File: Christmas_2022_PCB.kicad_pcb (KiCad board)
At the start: 2 copper layers, 61.4 x 60.5 mm, 45 parts, among them J1 USB_A, J2 SOP8_test_point, J3 SOP8_test_point, SW1 SW_Push, SW2 SW_Push, SW3 SW_SPDT, U1 STM32F030K6Tx, U2 AMS1117-3.3

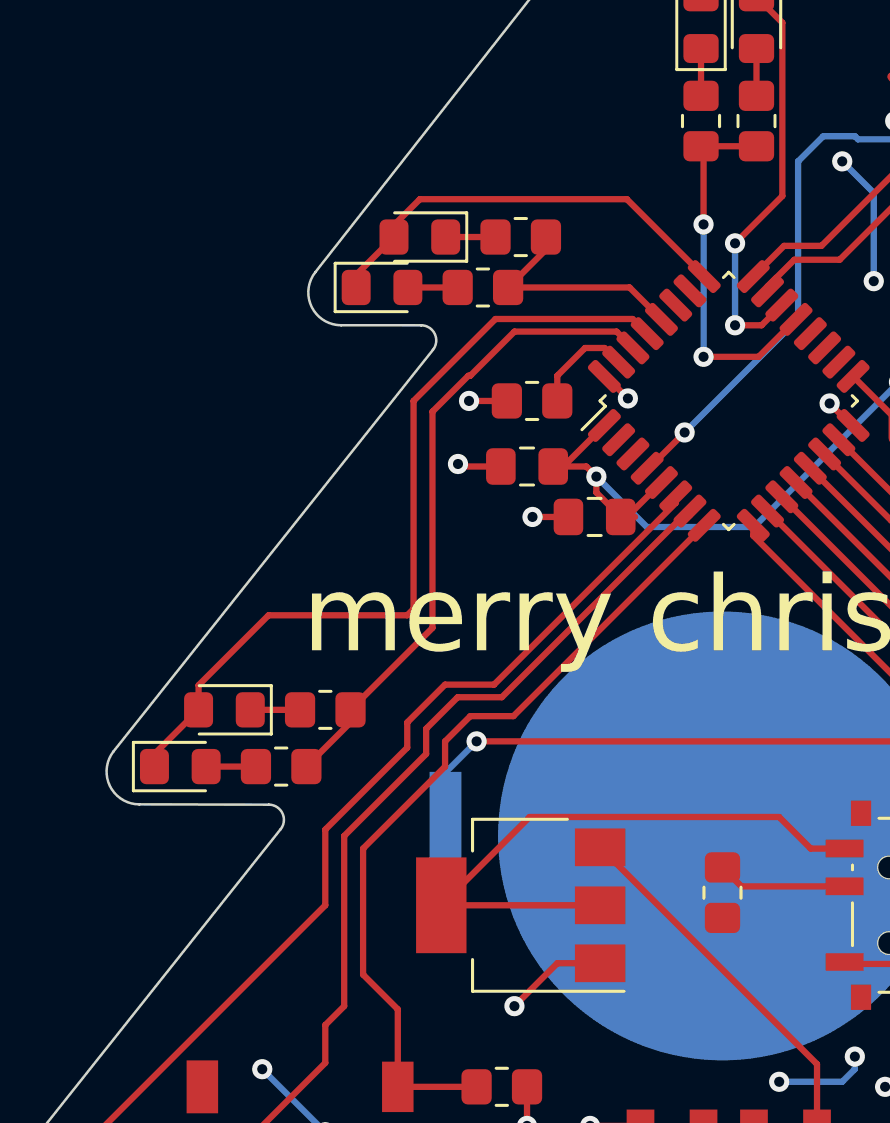
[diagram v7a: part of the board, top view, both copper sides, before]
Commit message: modified VCC pour to balance copper
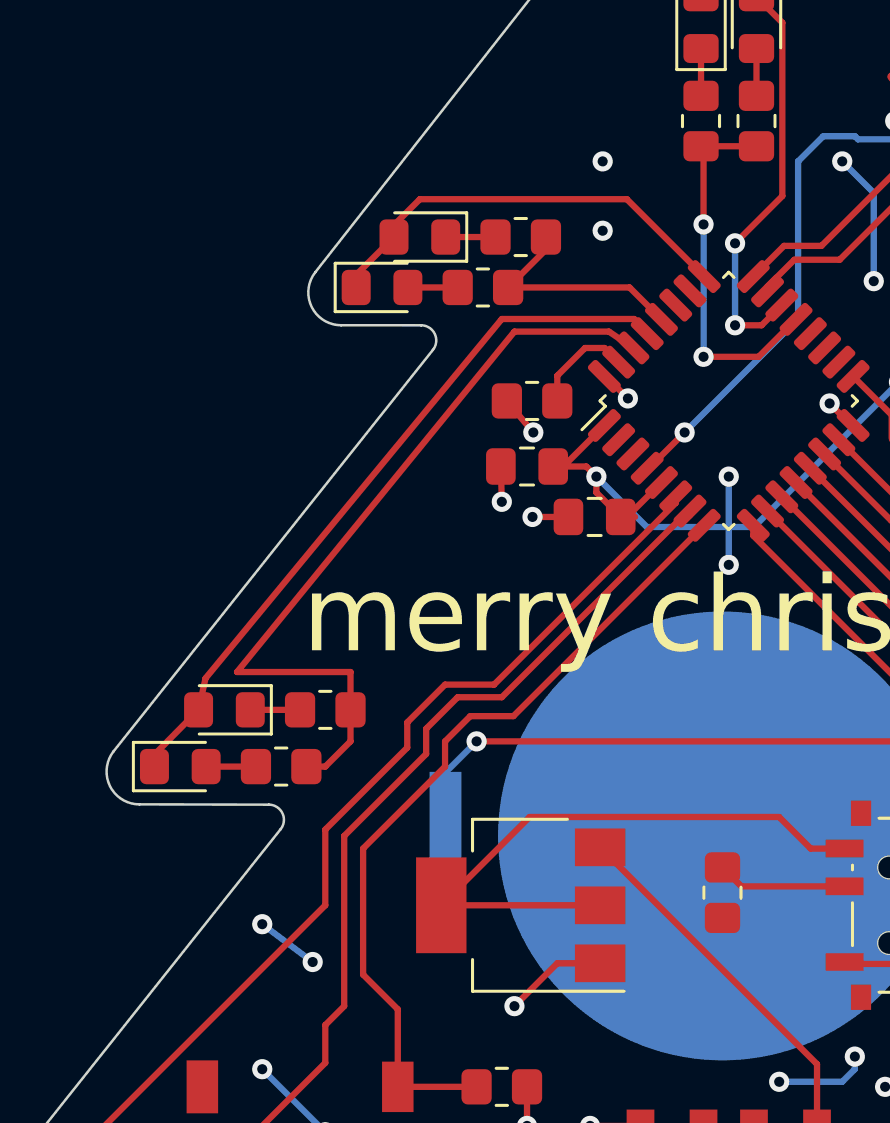
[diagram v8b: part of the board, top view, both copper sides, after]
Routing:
- net /LED7: track 25.7 -> 31.7 mm
- net +3V3: track 63.3 -> 69.3 mm, vias 11 -> 17
- net /LED8: track 32.8 -> 28.7 mm
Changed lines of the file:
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@@
   (segment (start 82 102.2) (end 82 103.75) (width 0.25) (layer "F.Cu") (net 2))
   (segment (start 94.93207 75.972272) (end 94.872272 75.972272) (width 0.25) (layer "F.Cu") (net 2))
+  (segment (start 81.2 75) (end 82.25 76.25) (width 0.25) (layer "F.Cu") (net 2))
   (segment (start 97.738821 62.761179) (end 96.6 63.9) (width 0.25) (layer "F.Cu") (net 2))
   (segment (start 98 102.2) (end 96.2 102.2) (width 0.25) (layer "F.Cu") (net 2))
@@
   (segment (start 94.872272 75.972272) (end 94 75.1) (width 0.25) (layer "F.Cu") (net 2))
   (segment (start 86.5 104.25) (end 86 103.75) (width 0.25) (layer "F.Cu") (net 2))
-  (segment (start 80.9625 77.6) (end 79.3625 77.6) (width 0.25) (layer "F.Cu") (net 2))
-  (segment (start 81.2 75) (end 79.7 75) (width 0.25) (layer "F.Cu") (net 2))
+  (segment (start 80.9625 77.6) (end 81 79) (width 0.25) (layer "F.Cu") (net 2))
   (segment (start 97.98189 62.761179) (end 97.738821 62.761179) (width 0.25) (layer "F.Cu") (net 2))
   (segment (start 85.06793 74.027728) (end 85.127728 74.027728) (width 0.25) (layer "F.Cu") (net 2))
@@
   (segment (start 83.642157 79.6) (end 82.217157 79.6) (width 0.25) (layer "F.Cu") (net 2))
   (segment (start 86 103.75) (end 84.5 103.75) (width 0.25) (layer "F.Cu") (net 2))
-  (segment (start 79.3625 77.6) (end 79.2625 77.5) (width 0.25) (layer "F.Cu") (net 2))
   (segment (start 86.5 104.35) (end 86.5 104.25) (width 0.25) (layer "F.Cu") (net 2))
   (via (at 100.4 76) (size 0.8) (drill 0.4) (layers "F.Cu" "B.Cu") (net 2))
   (via (at 96.6 63.9) (size 0.8) (drill 0.4) (layers "F.Cu" "B.Cu") (net 2))
-  (via (at 79.7 75) (size 0.8) (drill 0.4) (layers "F.Cu" "B.Cu") (net 2))
-  (via (at 79.2625 77.5) (size 0.8) (drill 0.4) (layers "F.Cu" "B.Cu") (net 2))
+  (via (at 82.25 76.25) (size 0.8) (drill 0.4) (layers "F.Cu" "B.Cu") (net 2))
+  (via (at 81 79) (size 0.8) (drill 0.4) (layers "F.Cu" "B.Cu") (net 2))
   (via (at 81.5 99) (size 0.8) (drill 0.4) (layers "F.Cu" "B.Cu") (net 2))
   (via (at 82.217157 79.6) (size 0.8) (drill 0.4) (layers "F.Cu" "B.Cu") (net 2))
@@
   (segment (start 85.717157 79.6) (end 85.965686 79.6) (width 0.25) (layer "F.Cu") (net 8))
   (via (at 94.5 65.5) (size 0.8) (drill 0.4) (layers "F.Cu" "B.Cu") (free) (net 8))
+  (via (at 90 78) (size 0.8) (drill 0.4) (layers "F.Cu" "B.Cu") (free) (net 8))
+  (via (at 90 81.5) (size 0.8) (drill 0.4) (layers "F.Cu" "B.Cu") (free) (net 8))
   (via (at 92 102) (size 0.8) (drill 0.4) (layers "F.Cu" "B.Cu") (free) (net 8))
+  (via (at 85 68.25) (size 0.8) (drill 0.4) (layers "F.Cu" "B.Cu") (free) (net 8))
   (via (at 105.25 103.25) (size 0.8) (drill 0.4) (layers "F.Cu" "B.Cu") (free) (net 8))
   (via (at 96.75 74.25) (size 0.8) (drill 0.4) (layers "F.Cu" "B.Cu") (net 8))
   (via (at 104.75 89.25) (size 0.8) (drill 0.4) (layers "F.Cu" "B.Cu") (net 8))
   (via (at 95 101) (size 0.8) (drill 0.4) (layers "F.Cu" "B.Cu") (free) (net 8))
+  (via (at 71.5 95.75) (size 0.8) (drill 0.4) (layers "F.Cu" "B.Cu") (free) (net 8))
+  (via (at 73.5 97.25) (size 0.8) (drill 0.4) (layers "F.Cu" "B.Cu") (free) (net 8))
   (via (at 95.75 70.25) (size 0.8) (drill 0.4) (layers "F.Cu" "B.Cu") (free) (net 8))
   (via (at 71.5 101.5) (size 0.8) (drill 0.4) (layers "F.Cu" "B.Cu") (free) (net 8))
   (via (at 84.75 78) (size 0.8) (drill 0.4) (layers "F.Cu" "B.Cu") (net 8))
   (via (at 74 104) (size 0.8) (drill 0.4) (layers "F.Cu" "B.Cu") (net 8))
+  (via (at 85 65.5) (size 0.8) (drill 0.4) (layers "F.Cu" "B.Cu") (free) (net 8))
   (via (at 108.5 99.5) (size 0.8) (drill 0.4) (layers "F.Cu" "B.Cu") (free) (net 8))
+  (segment (start 90 78) (end 90 81.5) (width 0.25) (layer "B.Cu") (net 8))
   (segment (start 96.75 74.25) (end 104.75 82.25) (width 0.25) (layer "B.Cu") (net 8))
   (segment (start 91 80) (end 96.75 74.25) (width 0.25) (layer "B.Cu") (net 8))
   (segment (start 95.75 66.75) (end 95.75 70.25) (width 0.25) (layer "B.Cu") (net 8))
   (segment (start 94.5 102) (end 92 102) (width 0.25) (layer "B.Cu") (net 8))
+  (segment (start 71.5 95.75) (end 73.5 97.25) (width 0.25) (layer "B.Cu") (net 8))
   (segment (start 108.5 100) (end 108.5 99.5) (width 0.25) (layer "B.Cu") (net 8))
   (segment (start 71.5 101.5) (end 74 104) (width 0.25) (layer "B.Cu") (net 8))
@@
   (segment (start 96.578427 78.75) (end 94.366384 76.537957) (width 0.25) (layer "F.Cu") (net 39))
   (segment (start 97.25 68.5) (end 98.75 70) (width 0.25) (layer "F.Cu") (net 39))
-  (segment (start 78.25 75.424695) (end 79.674695 74) (width 0.25) (layer "F.Cu") (net 40))
-  (segment (start 79.674695 74) (end 79.75 74) (width 0.25) (layer "F.Cu") (net 40))
-  (segment (start 75 87.75) (end 75 87.25) (width 0.25) (layer "F.Cu") (net 40))
-  (segment (start 78.25 84) (end 78.25 75.424695) (width 0.25) (layer "F.Cu") (net 40))
-  (segment (start 79.75 74) (end 81.5 72.25) (width 0.25) (layer "F.Cu") (net 40))
-  (segment (start 73.25 89.5) (end 75 87.75) (width 0.25) (layer "F.Cu") (net 40))
-  (segment (start 81.5 72.25) (end 85.552944 72.25) (width 0.25) (layer "F.Cu") (net 40))
-  (segment (start 85.552944 72.25) (end 86.199301 72.896357) (width 0.25) (layer "F.Cu") (net 40))
-  (segment (start 75 87.25) (end 78.25 84) (width 0.25) (layer "F.Cu") (net 40))
+  (segment (start 75 85.75) (end 70.5 85.75) (width 0.25) (layer "F.Cu") (net 40))
+  (segment (start 74 89.5) (end 75 88.5) (width 0.25) (layer "F.Cu") (net 40))
+  (segment (start 81.5 72.25) (end 85.25 72.25) (width 0.25) (layer "F.Cu") (net 40))
+  (segment (start 85.25 72.25) (end 86.199301 72.896357) (width 0.25) (layer "F.Cu") (net 40))
+  (segment (start 73.25 89.5) (end 74 89.5) (width 0.25) (layer "F.Cu") (net 40))
+  (segment (start 75 88.5) (end 75 87.25) (width 0.25) (layer "F.Cu") (net 40))
+  (segment (start 70.5 85.75) (end 81.5 72.25) (width 0.25) (layer "F.Cu") (net 40))
+  (segment (start 75 87.25) (end 75 85.75) (width 0.25) (layer "F.Cu") (net 40))
   (segment (start 101.684314 87.25) (end 92.669328 78.235014) (width 0.25) (layer "F.Cu") (net 41))
   (segment (start 106.75 89) (end 105 87.25) (width 0.25) (layer "F.Cu") (net 41))
@@
   (segment (start 76.725 68.5) (end 76.725 68.025) (width 0.25) (layer "F.Cu") (net 51))
   (segment (start 85.959798 67) (end 89.027728 70.06793) (width 0.25) (layer "F.Cu") (net 51))
-  (segment (start 68.975 86.275) (end 71.75 83.5) (width 0.25) (layer "F.Cu") (net 52))
-  (segment (start 68.975 87.25) (end 67.225 89) (width 0.25) (layer "F.Cu") (net 52))
-  (segment (start 77.25 83.5) (end 77.5 83.25) (width 0.25) (layer "F.Cu") (net 52))
-  (segment (start 77.5 83.25) (end 77.5 75) (width 0.25) (layer "F.Cu") (net 52))
-  (segment (start 80.75 71.75) (end 86.184314 71.75) (width 0.25) (layer "F.Cu") (net 52))
-  (segment (start 86.184314 71.75) (end 86.764986 72.330672) (width 0.25) (layer "F.Cu") (net 52))
-  (segment (start 67.225 89) (end 67.225 89.5) (width 0.25) (layer "F.Cu") (net 52))
-  (segment (start 71.75 83.5) (end 77.25 83.5) (width 0.25) (layer "F.Cu") (net 52))
-  (segment (start 77.5 75) (end 80.75 71.75) (width 0.25) (layer "F.Cu") (net 52))
-  (segment (start 68.975 87.25) (end 68.975 86.275) (width 0.25) (layer "F.Cu") (net 52))
+  (segment (start 68.975 87.25) (end 69.25 86) (width 0.25) (layer "F.Cu") (net 52))
+  (segment (start 86.25 71.75) (end 86.764986 72.330672) (width 0.25) (layer "F.Cu") (net 52))
+  (segment (start 67.225 89.5) (end 67.25 89) (width 0.25) (layer "F.Cu") (net 52))
+  (segment (start 81 71.75) (end 86.25 71.75) (width 0.25) (layer "F.Cu") (net 52))
+  (segment (start 67.25 89) (end 68.975 87.25) (width 0.25) (layer "F.Cu") (net 52))
+  (segment (start 69.25 86) (end 81 71.75) (width 0.25) (layer "F.Cu") (net 52))
   (zone (net 8) (net_name "+3V3") (layer "F.Cu") (hatch edge 0.508)
     (connect_pads (clearance 0.508))
     (min_thickness 0.254) (filled_areas_thickness no)
-    (fill yes (thermal_gap 0.508) (thermal_bridge_width 0.508))
+    (fill yes (thermal_gap 0.508) (thermal_bridge_width 0.508) (island_removal_mode 2) (island_area_min 5))
     (polygon
       (pts
